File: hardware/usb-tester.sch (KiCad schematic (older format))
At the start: 32 parts, among them J1 TARGET, J10 Target 1, J11 USB1, J12 SWD2, J13 Target 2, J14 USB2, J15 SWD3, J16 Target 3, J17 USB3, J2 Comm, J3 CommLA, J4 PowerMon, J5 Upstream, J6 SWD0, J7 Target 0, J8 USB0, J9 SWD1, U1 TLV1117-33, U2 STMPS2151STR, U3 USBLC6-2SC6, U4 CD74HC4067SM, U5 4514, U6 FSUSB30MUX, U7 FSUSB30MUX

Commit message: Use separate USBSEL signal for USB switches
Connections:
- net SEL0: no longer U6.1 (S), U7.1 (S)
- new net USBSEL: U6.1 (S), U7.1 (S)
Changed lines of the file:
@@
 USBMUXEN0
 Text Label 9900 7350 2    50   ~ 0
-SEL0
+USBSEL
 Text Label 9900 6750 2    50   ~ 0
 T0_USB_D+
@@
 USBMUXEN1
 Text Label 11650 7350 2    50   ~ 0
-SEL0
+USBSEL
 $Comp
 L Connector:Conn_01x03_Male J8
@@
 Wire Wire Line
 	8700 1200 8800 1200
+Text Label 9500 2350 2    50   ~ 0
+USBSEL
 $EndSCHEMATC

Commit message: WIP main board layout
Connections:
- net GND: now also J5.1 (Pin_1); no longer J5.3 (Pin_3)
- net USB_D+: now also J5.3 (Pin_3), U3.1 (IO1); no longer J5.1 (Pin_1), U3.3 (IO2)
- net USB_D-: now also U3.3 (IO2); no longer U3.1 (IO1)
- net at U3.4 (IO2): now also J1.2 (D-); no longer J1.3 (D+)
- net at U3.6 (IO1): now also J1.3 (D+); no longer J1.2 (D-)
- net VIN: now reaches C1.1, JP1.2 (C), U1.3 (VI)
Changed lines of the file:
@@
 U 1 1 5E3FD4F5
 P 2300 1700
-F 0 "U3" H 2050 2050 50  0000 C CNN
-F 1 "USBLC6-2SC6" H 2600 2050 50  0000 C CNN
+F 0 "U3" H 2300 2381 50  0000 C CNN
+F 1 "USBLC6-2SC6" H 2300 2290 50  0000 C CNN
 F 2 "Package_TO_SOT_SMD:SOT-23-6" H 1550 2100 50  0001 C CNN
 F 3 "http://www2.st.com/resource/en/datasheet/CD00050750.pdf" H 2500 2050 50  0001 C CNN
 	1    2300 1700
-	1    0    0    -1
+	-1   0    0    -1
 $EndComp
 $Comp
@@
 F 3 "~" H 1650 2550 50  0001 C CNN
 	1    1650 2550
-	-1   0    0    1
+	-1   0    0    -1
 $EndComp
 Text Label 1450 2550 2    50   ~ 0
@@
 Text Label 9500 2350 2    50   ~ 0
 USBSEL
+Text Label 4400 1100 2    50   ~ 0
+VIN
 $EndSCHEMATC

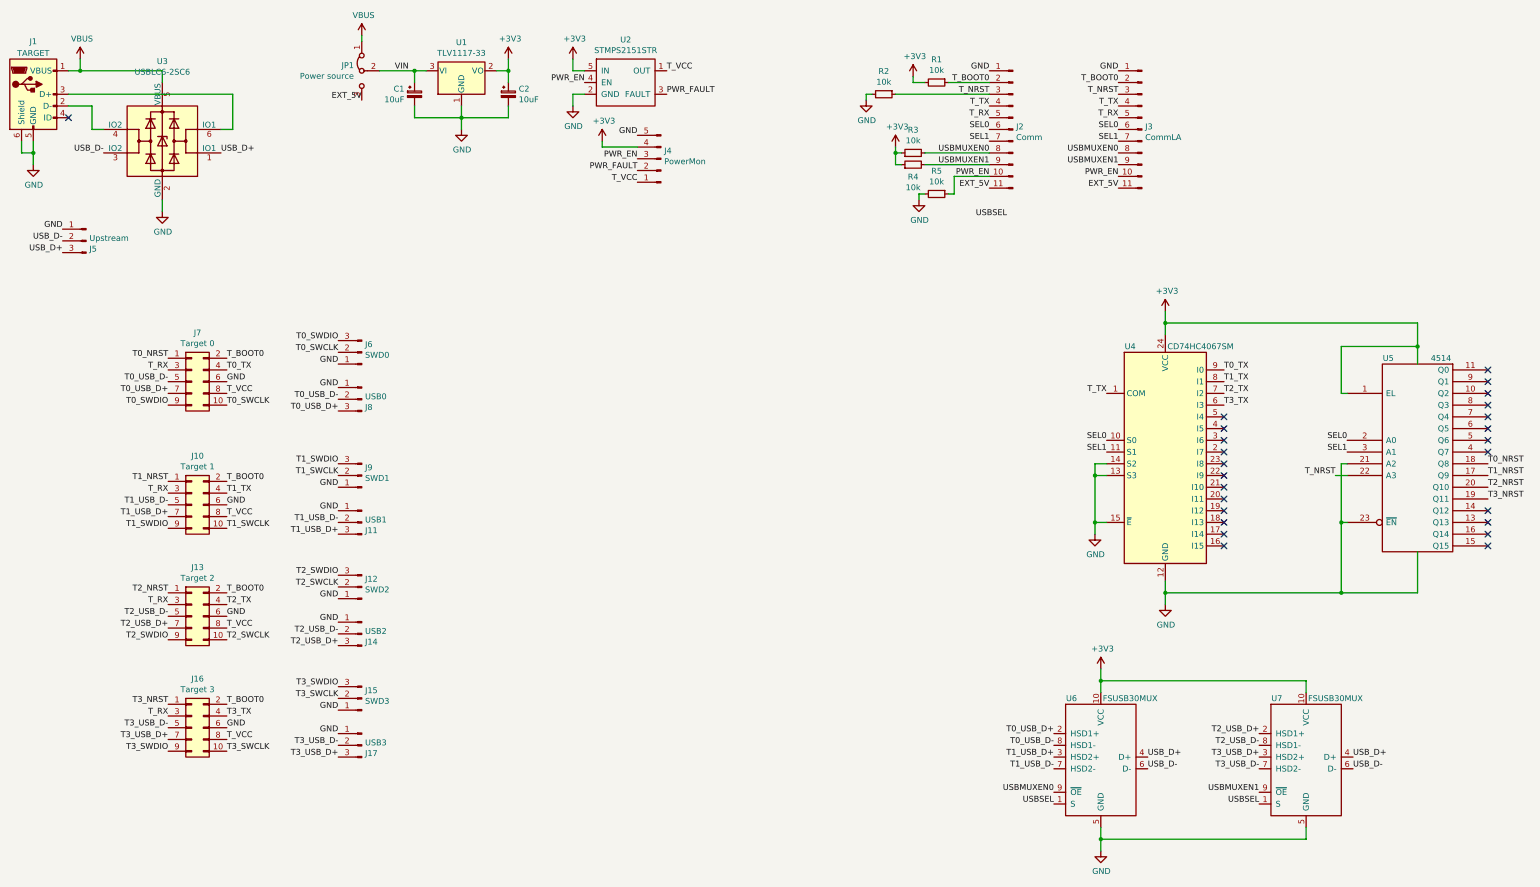
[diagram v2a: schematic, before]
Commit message: Simplify schematics, add WIP layout
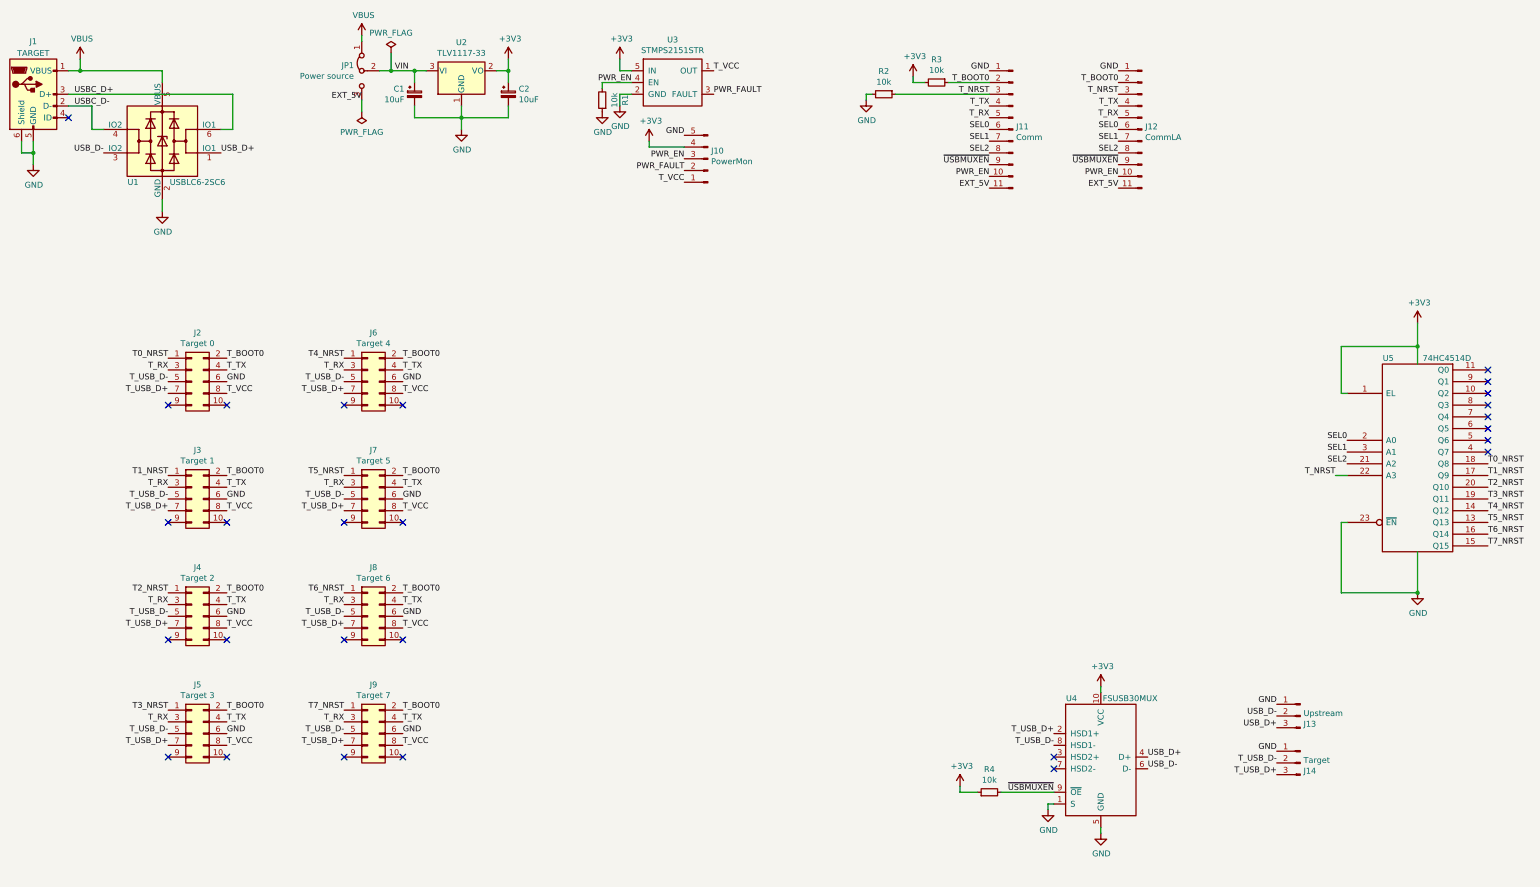
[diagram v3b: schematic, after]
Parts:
- removed J11: USB1, Connector_PinHeader_2.54mm:PinHeader_1x03_P2.54mm_Vertical, symbol Connector:Conn_01x03_Male
- removed J12: SWD2, Connector_PinHeader_2.54mm:PinHeader_1x03_P2.54mm_Vertical, symbol Connector:Conn_01x03_Male
- removed J14: USB2, Connector_PinHeader_2.54mm:PinHeader_1x03_P2.54mm_Vertical, symbol Connector:Conn_01x03_Male
- removed J15: SWD3, Connector_PinHeader_2.54mm:PinHeader_1x03_P2.54mm_Vertical, symbol Connector:Conn_01x03_Male
- removed J17: USB3, Connector_PinHeader_2.54mm:PinHeader_1x03_P2.54mm_Vertical, symbol Connector:Conn_01x03_Male
- removed J6: SWD0, Connector_PinHeader_2.54mm:PinHeader_1x03_P2.54mm_Vertical, symbol Connector:Conn_01x03_Male
- removed J9: SWD1, Connector_PinHeader_2.54mm:PinHeader_1x03_P2.54mm_Vertical, symbol Connector:Conn_01x03_Male
- removed R4: 10k, Resistor_SMD:R_1206_3216Metric_Pad1.42x1.75mm_HandSolder, symbol Device:R_Small
- removed U4: CD74HC4067SM, Package_SO:SSOP-24_5.3x8.2mm_P0.65mm, symbol 74xx:CD74HC4067SM
- removed U7: FSUSB30MUX, Package_SO:MSOP-10_3x3mm_P0.5mm, symbol ic:FSUSB30MUX
- added J6: Target 4, Connector_PinSocket_2.54mm:PinSocket_2x05_P2.54mm_Vertical, symbol Connector_Generic:Conn_02x05_Odd_Even
- added J7: Target 5, Connector_PinSocket_2.54mm:PinSocket_2x05_P2.54mm_Vertical, symbol Connector_Generic:Conn_02x05_Odd_Even
- added J8: Target 6, Connector_PinSocket_2.54mm:PinSocket_2x05_P2.54mm_Vertical, symbol Connector_Generic:Conn_02x05_Odd_Even
- added J9: Target 7, Connector_PinSocket_2.54mm:PinSocket_2x05_P2.54mm_Vertical, symbol Connector_Generic:Conn_02x05_Odd_Even
- J14: renamed from J8; value USB0 -> Target
- U5: value 4514 -> 74HC4514D
- renumbered J4 to J10, J2 to J11, J3 to J12, J5 to J13, J7 to J2, J10 to J3, J13 to J4, J16 to J5, R5 to R1, R1 to R3, R3 to R4, U3 to U1, U1 to U2, U2 to U3, U6 to U4
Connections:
- net T0_TX is gone; now on net T_TX: J2.4 (Pin_4)
- net T1_TX is gone; now on net T_TX: J3.4 (Pin_4)
- net T2_TX is gone; now on net T_TX: J4.4 (Pin_4)
- net T2_USB_D+ is gone; now on net T_USB_D+: J4.7 (Pin_7)
- net T2_USB_D- is gone; now on net T_USB_D-: J4.5 (Pin_5)
- net T3_TX is gone; now on net T_TX: J5.4 (Pin_4)
- net T3_USB_D+ is gone; now on net T_USB_D+: J5.7 (Pin_7)
- net T3_USB_D- is gone; now on net T_USB_D-: J5.5 (Pin_5)
- net USBSEL is gone; now on net GND: U4.1 (S)
- net GND: now also R1.1, J6.6 (Pin_6), J7.6 (Pin_6), J8.6 (Pin_6), J9.6 (Pin_6); no longer R1.2, U5.21 (A2)
- net PWR_EN: now also R1.2; no longer R1.1
- net T_BOOT0: now also J6.2 (Pin_2), J7.2 (Pin_2), J8.2 (Pin_2), J9.2 (Pin_2)
- net T_RX: now also J6.3 (Pin_3), J7.3 (Pin_3), J8.3 (Pin_3), J9.3 (Pin_3)
- net T_TX: now also J6.4 (Pin_4), J7.4 (Pin_4), J8.4 (Pin_4), J9.4 (Pin_4)
- net T_VCC: now also J6.8 (Pin_8), J7.8 (Pin_8), J8.8 (Pin_8), J9.8 (Pin_8)
- net USBC_D-: now reaches J1.2 (D-), U1.4 (IO2)
- net USBC_D+: now reaches J1.3 (D+), U1.6 (IO1)
- net T5_NRST: now reaches U5.13 (Q13)
- net T5_NRST: now also J7.1 (Pin_1)
- net T4_NRST: now reaches U5.14 (Q12)
- net T4_NRST: now also J6.1 (Pin_1)
- net T7_NRST: now reaches U5.15 (Q15)
- net T7_NRST: now also J9.1 (Pin_1)
- net T6_NRST: now reaches U5.16 (Q14)
- net T6_NRST: now also J8.1 (Pin_1)
- net T0_SWCLK: no longer names the net of J2.10 (Pin_10)
- net T0_SWDIO: no longer names the net of J2.9 (Pin_9)
- net T0_USB_D+ renamed T_USB_D+
- net T_USB_D+: now also J3.7 (Pin_7), J6.7 (Pin_7), J7.7 (Pin_7), J8.7 (Pin_7), J9.7 (Pin_7)
- net T0_USB_D- renamed T_USB_D-
- net T_USB_D-: now also J3.5 (Pin_5), J6.5 (Pin_5), J7.5 (Pin_5), J8.5 (Pin_5), J9.5 (Pin_5)
- net T1_SWCLK: no longer names the net of J3.10 (Pin_10)
- net T1_SWDIO: no longer names the net of J3.9 (Pin_9)
- net T1_USB_D+: no longer names the net of U4.3 (HSD2+)
- net T1_USB_D+: no longer J3.7 (Pin_7)
- net T1_USB_D-: no longer names the net of U4.7 (HSD2-)
- net T1_USB_D-: no longer J3.5 (Pin_5)
- net T2_SWCLK: no longer names the net of J4.10 (Pin_10)
- net T2_SWDIO: no longer names the net of J4.9 (Pin_9)
- net T3_SWCLK: no longer names the net of J5.10 (Pin_10)
- net T3_SWDIO: no longer names the net of J5.9 (Pin_9)
- net USBMUXEN0 renamed SEL2
- net SEL2: now also U5.21 (A2); no longer R4.2, U4.9 (~OE)
- net USBMUXEN1 renamed ~USBMUXEN
- net ~USBMUXEN: now also R4.2, U4.9 (~OE)
- no-connect marks 25 -> 27
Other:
- moved on the sheet: J10, J13, J14, J3, J5, R1, R4, U3

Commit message: Finalize shematics and layout
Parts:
- removed C1, C2: 10uF, Capacitor_Tantalum_SMD:CP_EIA-3216-18_Kemet-A_Pad1.58x1.35mm_HandSolder, symbol Device:CP_Small
- removed J10: PowerMon, Connector_PinHeader_2.54mm:PinHeader_1x05_P2.54mm_Vertical, symbol Connector:Conn_01x05_Male
- removed JP1: Power source, Connector_PinHeader_2.54mm:PinHeader_1x03_P2.54mm_Vertical, symbol Jumper:Jumper_3_Bridged12
- removed U2: TLV1117-33, Package_TO_SOT_SMD:SOT-223-3_TabPin2, symbol Regulator_Linear:TLV1117-33
- added J15: Idd, Connector_PinHeader_2.54mm:PinHeader_1x02_P2.54mm_Vertical, symbol Connector:Conn_01x02_Male
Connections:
- net EXT_5V is gone; now on net T_BOOT0: J11.11 (Pin_11), J12.11 (Pin_11)
- net +3V3: now also J11.1 (Pin_1), J12.1 (Pin_1); no longer R3.2
- net GND: now also J11.2 (Pin_2), J12.2 (Pin_2); no longer J11.1 (Pin_1), J12.1 (Pin_1)
- net PWR_EN: now also J11.8 (Pin_8), J12.8 (Pin_8); no longer J11.10 (Pin_10), J12.10 (Pin_10)
- net SEL0: now also J11.4 (Pin_4), J12.4 (Pin_4); no longer J11.6 (Pin_6), J12.6 (Pin_6)
- net SEL1: now also J11.5 (Pin_5), J12.5 (Pin_5); no longer J11.7 (Pin_7), J12.7 (Pin_7)
- net SEL2: now also J11.6 (Pin_6), J12.6 (Pin_6); no longer J11.8 (Pin_8), J12.8 (Pin_8)
- net T0_NRST: now also U5.17 (Q9); no longer U5.18 (Q8)
- net T1_NRST: now also U5.13 (Q13); no longer U5.17 (Q9)
- net T2_NRST: now also U5.18 (Q8); no longer U5.20 (Q10)
- net T3_NRST: now also U5.14 (Q12); no longer U5.19 (Q11)
- net T4_NRST: now also U5.19 (Q11); no longer U5.14 (Q12)
- net T5_NRST: now also U5.15 (Q15); no longer U5.13 (Q13)
- net T6_NRST: now also U5.20 (Q10); no longer U5.16 (Q14)
- net T7_NRST: now also U5.16 (Q14); no longer U5.15 (Q15)
- net T_BOOT0: no longer J11.2 (Pin_2), J12.2 (Pin_2)
- net T_RX: now also J11.9 (Pin_9), J12.9 (Pin_9); no longer J11.5 (Pin_5), J12.5 (Pin_5)
- net T_TX: now also J11.10 (Pin_10), J12.10 (Pin_10); no longer J11.4 (Pin_4), J12.4 (Pin_4)
- net T_VCC: now also R3.2, J15.2 (Pin_2); no longer U3.1 (OUT)
- net ~USBMUXEN: now also J11.7 (Pin_7), J12.7 (Pin_7); no longer J11.9 (Pin_9), J12.9 (Pin_9)
- new net T_VCC_SRC: J15.1 (Pin_1), U3.1 (OUT)
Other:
- moved on the sheet: R1, R3

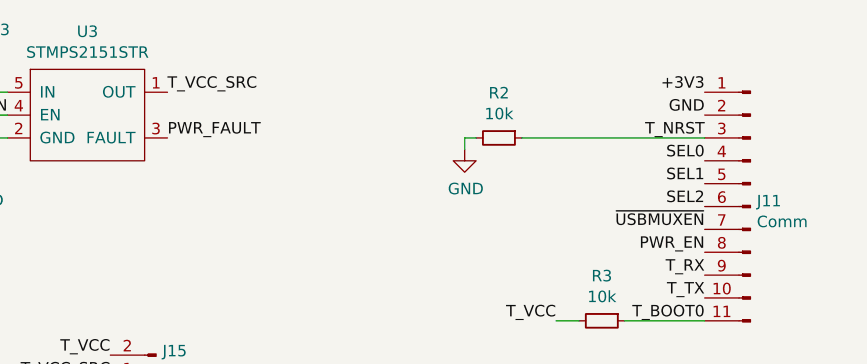
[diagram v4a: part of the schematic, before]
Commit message: Fix ERC errors
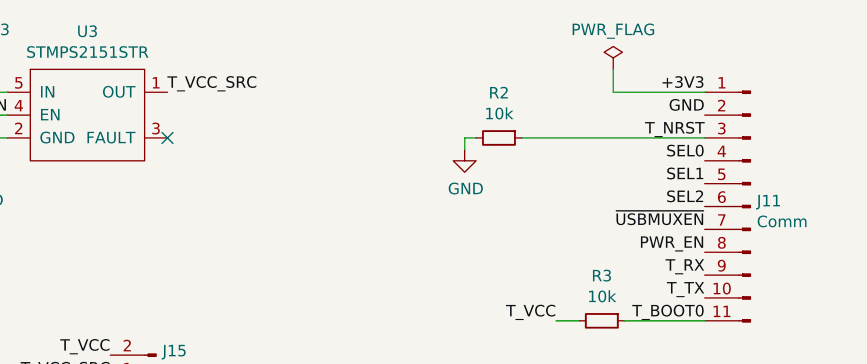
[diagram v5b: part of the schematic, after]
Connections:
- net PWR_FAULT: no longer names the net of U3.3 (FAULT)
- no-connect marks 27 -> 28
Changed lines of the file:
@@
 	-1   0    0    1
 $EndComp
-Text Label 7000 1300 0    50   ~ 0
-PWR_FAULT
 Text Label 7000 1100 0    50   ~ 0
 T_VCC_SRC
@@
 Text Label 1550 1100 0    50   ~ 0
 VBUS
+$Comp
+L power:PWR_FLAG #FLG0101
+U 1 1 5EC7CCD7
+P 8950 1000
+F 0 "#FLG0101" H 8950 1075 50  0001 C CNN
+F 1 "PWR_FLAG" H 8950 1173 50  0000 C CNN
+F 2 "" H 8950 1000 50  0001 C CNN
+F 3 "~" H 8950 1000 50  0001 C CNN
+	1    8950 1000
+	1    0    0    -1
+$EndComp
+Wire Wire Line
+	8950 1000 8950 1100
+Wire Wire Line
+	8950 1100 9350 1100
+NoConn ~ 7000 1300
 $EndSCHEMATC

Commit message: Use reversed footprint instead of a standard one
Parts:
- J2, J3, J4, J5, J6, J7, J8, J9: footprint Connector_PinSocket_2.54mm:PinSocket_2x05_P2.54mm_Vertical -> unsorted:PinSocket_2x05_P2.54mm_Vertical_Reversed
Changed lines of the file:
@@
 F 0 "J2" H 2600 4167 50  0000 C CNN
 F 1 "Target 0" H 2600 4076 50  0000 C CNN
-F 2 "Connector_PinSocket_2.54mm:PinSocket_2x05_P2.54mm_Vertical" H 2550 3750 50  0001 C CNN
+F 2 "unsorted:PinSocket_2x05_P2.54mm_Vertical_Reversed" H 2550 3750 50  0001 C CNN
 F 3 "~" H 2550 3750 50  0001 C CNN
 	1    2550 3750
@@
 F 0 "J3" H 2600 5167 50  0000 C CNN
 F 1 "Target 1" H 2600 5076 50  0000 C CNN
-F 2 "Connector_PinSocket_2.54mm:PinSocket_2x05_P2.54mm_Vertical" H 2550 4750 50  0001 C CNN
+F 2 "unsorted:PinSocket_2x05_P2.54mm_Vertical_Reversed" H 2550 4750 50  0001 C CNN
 F 3 "~" H 2550 4750 50  0001 C CNN
 	1    2550 4750
@@
 F 0 "J4" H 2600 6167 50  0000 C CNN
 F 1 "Target 2" H 2600 6076 50  0000 C CNN
-F 2 "Connector_PinSocket_2.54mm:PinSocket_2x05_P2.54mm_Vertical" H 2550 5750 50  0001 C CNN
+F 2 "unsorted:PinSocket_2x05_P2.54mm_Vertical_Reversed" H 2550 5750 50  0001 C CNN
 F 3 "~" H 2550 5750 50  0001 C CNN
 	1    2550 5750
@@
 F 0 "J5" H 2600 7167 50  0000 C CNN
 F 1 "Target 3" H 2600 7076 50  0000 C CNN
-F 2 "Connector_PinSocket_2.54mm:PinSocket_2x05_P2.54mm_Vertical" H 2550 6750 50  0001 C CNN
+F 2 "unsorted:PinSocket_2x05_P2.54mm_Vertical_Reversed" H 2550 6750 50  0001 C CNN
 F 3 "~" H 2550 6750 50  0001 C CNN
 	1    2550 6750
@@
 F 0 "J6" H 4100 4167 50  0000 C CNN
 F 1 "Target 4" H 4100 4076 50  0000 C CNN
-F 2 "Connector_PinSocket_2.54mm:PinSocket_2x05_P2.54mm_Vertical" H 4050 3750 50  0001 C CNN
+F 2 "unsorted:PinSocket_2x05_P2.54mm_Vertical_Reversed" H 4050 3750 50  0001 C CNN
 F 3 "~" H 4050 3750 50  0001 C CNN
 	1    4050 3750
@@
 F 0 "J7" H 4100 5167 50  0000 C CNN
 F 1 "Target 5" H 4100 5076 50  0000 C CNN
-F 2 "Connector_PinSocket_2.54mm:PinSocket_2x05_P2.54mm_Vertical" H 4050 4750 50  0001 C CNN
+F 2 "unsorted:PinSocket_2x05_P2.54mm_Vertical_Reversed" H 4050 4750 50  0001 C CNN
 F 3 "~" H 4050 4750 50  0001 C CNN
 	1    4050 4750
@@
 F 0 "J8" H 4100 6167 50  0000 C CNN
 F 1 "Target 6" H 4100 6076 50  0000 C CNN
-F 2 "Connector_PinSocket_2.54mm:PinSocket_2x05_P2.54mm_Vertical" H 4050 5750 50  0001 C CNN
+F 2 "unsorted:PinSocket_2x05_P2.54mm_Vertical_Reversed" H 4050 5750 50  0001 C CNN
 F 3 "~" H 4050 5750 50  0001 C CNN
 	1    4050 5750
@@
 F 0 "J9" H 4100 7167 50  0000 C CNN
 F 1 "Target 7" H 4100 7076 50  0000 C CNN
-F 2 "Connector_PinSocket_2.54mm:PinSocket_2x05_P2.54mm_Vertical" H 4050 6750 50  0001 C CNN
+F 2 "unsorted:PinSocket_2x05_P2.54mm_Vertical_Reversed" H 4050 6750 50  0001 C CNN
 F 3 "~" H 4050 6750 50  0001 C CNN
 	1    4050 6750
